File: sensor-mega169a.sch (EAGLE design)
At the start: 55 parts, among them IC3 ATmega169PA, K1 SP6029TOP, M1 NRF24L01P-M, M2 DHT22, Q1 IRLML2502, Q2 IRLML2502, Q3 IRLML6402, U1 MCP1640C, U2 MCP604-I/ST

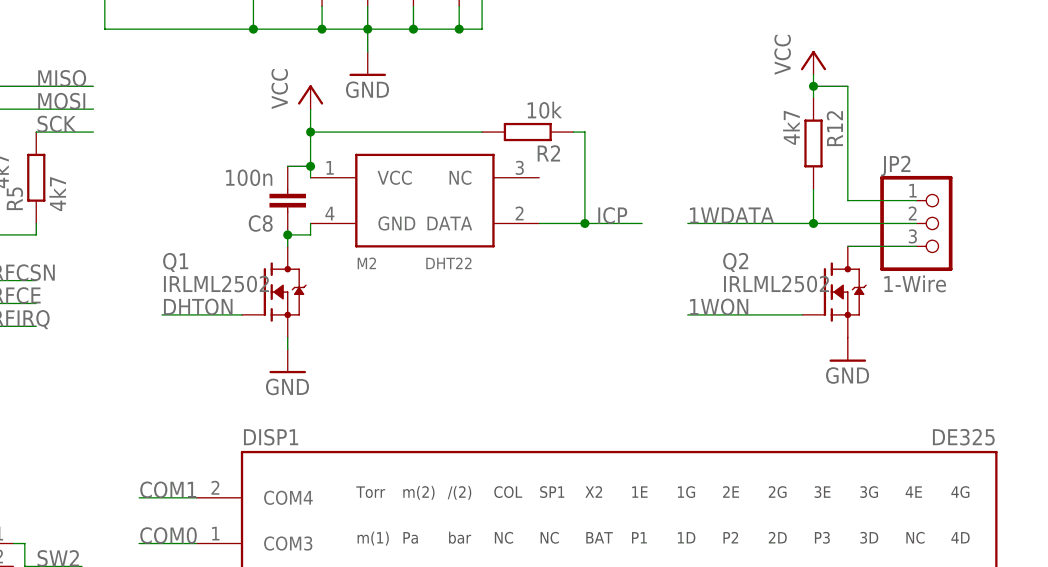
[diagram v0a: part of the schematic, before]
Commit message: changed irlml* parts to own library with better footprint
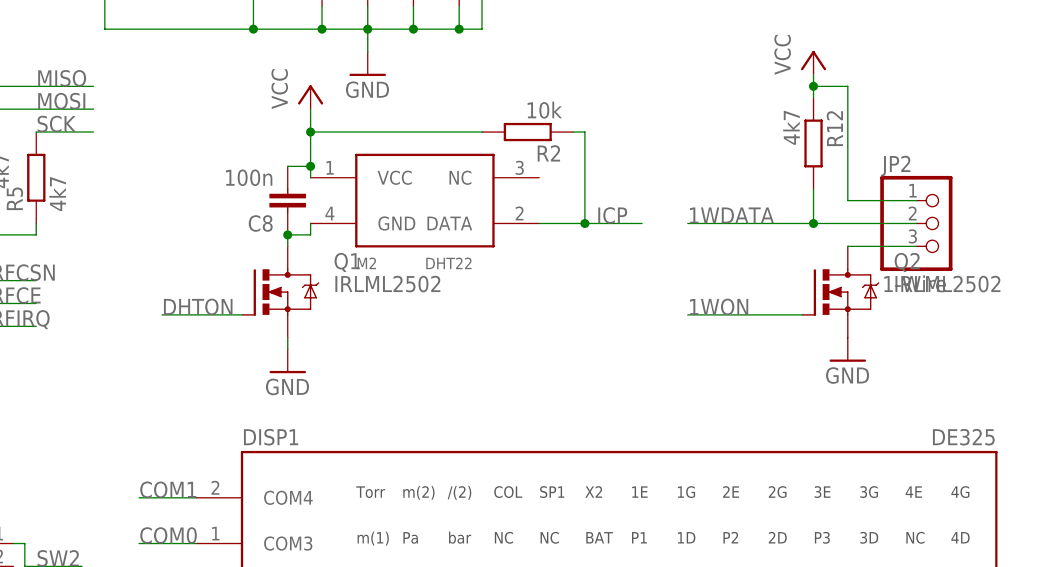
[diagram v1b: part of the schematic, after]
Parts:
- Q1, Q2: device xmaker:IRLML2502 -> mosfet:IRLML2502
- Q3: device transistor-power:IRLML5203 -> mosfet:IRLML6402
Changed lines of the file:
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@@
 <setting verticaltext="up"/>
 </settings>
-<grid distance="1.27" unitdist="mm" unit="mm" style="lines" multiple="1" display="yes" altdistance="635" altunitdist="mic" altunit="mic"/>
+<grid distance="0.1" unitdist="inch" unit="mm" style="lines" multiple="1" display="yes" altdistance="0.01" altunitdist="inch" altunit="mm"/>
 <layers>
-<layer number="1" name="Top" color="4" fill="1" visible="yes" active="no"/>
-<layer number="2" name="Route2" color="1" fill="3" visible="yes" active="no"/>
-<layer number="3" name="Route3" color="4" fill="3" visible="yes" active="no"/>
-<layer number="4" name="Route4" color="1" fill="4" visible="yes" active="no"/>
-<layer number="5" name="Route5" color="4" fill="4" visible="yes" active="no"/>
-<layer number="6" name="Route6" color="1" fill="8" visible="yes" active="no"/>
-<layer number="7" name="Route7" color="4" fill="8" visible="yes" active="no"/>
-<layer number="8" name="Route8" color="1" fill="2" visible="yes" active="no"/>
-<layer number="9" name="Route9" color="4" fill="2" visible="yes" active="no"/>
-<layer number="10" name="Route10" color="1" fill="7" visible="yes" active="no"/>
-<layer number="11" name="Route11" color="4" fill="7" visible="yes" active="no"/>
-<layer number="12" name="Route12" color="1" fill="5" visible="yes" active="no"/>
-<layer number="13" name="Route13" color="4" fill="5" visible="yes" active="no"/>
-<layer number="14" name="Route14" color="1" fill="6" visible="yes" active="no"/>
-<layer number="15" name="Route15" color="4" fill="6" visible="yes" active="no"/>
-<layer number="16" name="Bottom" color="1" fill="1" visible="yes" active="no"/>
-<layer number="17" name="Pads" color="2" fill="1" visible="yes" active="no"/>
-<layer number="18" name="Vias" color="2" fill="1" visible="yes" active="no"/>
-<layer number="19" name="Unrouted" color="6" fill="1" visible="yes" active="no"/>
-<layer number="20" name="Dimension" color="15" fill="1" visible="yes" active="no"/>
-<layer number="21" name="tPlace" color="7" fill="1" visible="yes" active="no"/>
-<layer number="22" name="bPlace" color="7" fill="1" visible="yes" active="no"/>
-<layer number="23" name="tOrigins" color="15" fill="1" visible="yes" active="no"/>
-<layer number="24" name="bOrigins" color="15" fill="1" visible="yes" active="no"/>
-<layer number="25" name="tNames" color="7" fill="1" visible="yes" active="no"/>
-<layer number="26" name="bNames" color="7" fill="1" visible="yes" active="no"/>
-<layer number="27" name="tValues" color="7" fill="1" visible="yes" active="no"/>
-<layer number="28" name="bValues" color="7" fill="1" visible="yes" active="no"/>
+<layer number="1" name="Top" color="4" fill="1" visible="no" active="no"/>
+<layer number="2" name="Route2" color="1" fill="3" visible="no" active="no"/>
+<layer number="3" name="Route3" color="4" fill="3" visible="no" active="no"/>
+<layer number="4" name="Route4" color="1" fill="4" visible="no" active="no"/>
+<layer number="5" name="Route5" color="4" fill="4" visible="no" active="no"/>
+<layer number="6" name="Route6" color="1" fill="8" visible="no" active="no"/>
+<layer number="7" name="Route7" color="4" fill="8" visible="no" active="no"/>
+<layer number="8" name="Route8" color="1" fill="2" visible="no" active="no"/>
+<layer number="9" name="Route9" color="4" fill="2" visible="no" active="no"/>
+<layer number="10" name="Route10" color="1" fill="7" visible="no" active="no"/>
+<layer number="11" name="Route11" color="4" fill="7" visible="no" active="no"/>
+<layer number="12" name="Route12" color="1" fill="5" visible="no" active="no"/>
+<layer number="13" name="Route13" color="4" fill="5" visible="no" active="no"/>
+<layer number="14" name="Route14" color="1" fill="6" visible="no" active="no"/>
+<layer number="15" name="Route15" color="4" fill="6" visible="no" active="no"/>
+<layer number="16" name="Bottom" color="1" fill="1" visible="no" active="no"/>
+<layer number="17" name="Pads" color="2" fill="1" visible="no" active="no"/>
+<layer number="18" name="Vias" color="2" fill="1" visible="no" active="no"/>
+<layer number="19" name="Unrouted" color="6" fill="1" visible="no" active="no"/>
+<layer number="20" name="Dimension" color="15" fill="1" visible="no" active="no"/>
+<layer number="21" name="tPlace" color="7" fill="1" visible="no" active="no"/>
+<layer number="22" name="bPlace" color="7" fill="1" visible="no" active="no"/>
+<layer number="23" name="tOrigins" color="15" fill="1" visible="no" active="no"/>
+<layer number="24" name="bOrigins" color="15" fill="1" visible="no" active="no"/>
+<layer number="25" name="tNames" color="7" fill="1" visible="no" active="no"/>
+<layer number="26" name="bNames" color="7" fill="1" visible="no" active="no"/>
+<layer number="27" name="tValues" color="7" fill="1" visible="no" active="no"/>
+<layer number="28" name="bValues" color="7" fill="1" visible="no" active="no"/>
 <layer number="29" name="tStop" color="7" fill="3" visible="no" active="no"/>
 <layer number="30" name="bStop" color="7" fill="6" visible="no" active="no"/>
@@
 <layer number="35" name="tGlue" color="7" fill="4" visible="no" active="no"/>
 <layer number="36" name="bGlue" color="7" fill="5" visible="no" active="no"/>
-<layer number="37" name="tTest" color="7" fill="1" visible="yes" active="no"/>
-<layer number="38" name="bTest" color="7" fill="1" visible="yes" active="no"/>
+<layer number="37" name="tTest" color="7" fill="1" visible="no" active="no"/>
+<layer number="38" name="bTest" color="7" fill="1" visible="no" active="no"/>
 <layer number="39" name="tKeepout" color="4" fill="11" visible="no" active="no"/>
 <layer number="40" name="bKeepout" color="1" fill="11" visible="no" active="no"/>
@@
 <layer number="44" name="Drills" color="7" fill="1" visible="no" active="no"/>
 <layer number="45" name="Holes" color="7" fill="1" visible="no" active="no"/>
-<layer number="46" name="Milling" color="3" fill="1" visible="yes" active="no"/>
-<layer number="47" name="Measures" color="7" fill="1" visible="yes" active="no"/>
-<layer number="48" name="Document" color="7" fill="1" visible="yes" active="no"/>
-<layer number="49" name="Reference" color="7" fill="1" visible="yes" active="no"/>
-<layer number="50" name="dxf" color="7" fill="1" visible="yes" active="no"/>
-<layer number="51" name="tDocu" color="7" fill="1" visible="yes" active="no"/>
-<layer number="52" name="bDocu" color="7" fill="1" visible="yes" active="no"/>
-<layer number="53" name="tGND_GNDA" color="7" fill="9" visible="yes" active="no"/>
-<layer number="54" name="bGND_GNDA" color="1" fill="9" visible="yes" active="no"/>
-<layer number="56" name="wert" color="7" fill="1" visible="yes" active="no"/>
+<layer number="46" name="Milling" color="3" fill="1" visible="no" active="no"/>
+<layer number="47" name="Measures" color="7" fill="1" visible="no" active="no"/>
+<layer number="48" name="Document" color="7" fill="1" visible="no" active="no"/>
+<layer number="49" name="Reference" color="7" fill="1" visible="no" active="no"/>
+<layer number="50" name="dxf" color="7" fill="1" visible="no" active="no"/>
+<layer number="51" name="tDocu" color="7" fill="1" visible="no" active="no"/>
+<layer number="52" name="bDocu" color="7" fill="1" visible="no" active="no"/>
+<layer number="53" name="tGND_GNDA" color="7" fill="9" visible="no" active="no"/>
+<layer number="54" name="bGND_GNDA" color="1" fill="9" visible="no" active="no"/>
+<layer number="56" name="wert" color="7" fill="1" visible="no" active="no"/>
 <layer number="91" name="Nets" color="2" fill="1" visible="yes" active="yes"/>
 <layer number="92" name="Busses" color="1" fill="1" visible="yes" active="yes"/>
@@
 <part name="R10" library="rcl" deviceset="R-EU_" device="R0603" value="270k"/>
 <part name="P+2" library="supply1" deviceset="VCC" device=""/>
-<part name="Q1" library="xmaker" deviceset="IRLML2502" device=""/>
+<part name="Q1" library="mosfet" deviceset="IRLML2502" device=""/>
 <part name="JP1" library="pinhead-mod" deviceset="PINHD-1X2" device="_2.54" value="I2C"/>
 <part name="JP2" library="pinhead-mod" deviceset="PINHD-1X3" device="_2.54" value="1-Wire"/>
@@
 <part name="R11" library="rcl" deviceset="R-EU_" device="R0603" value="4k7"/>
 <part name="P+5" library="supply1" deviceset="VCC" device=""/>
-<part name="Q2" library="xmaker" deviceset="IRLML2502" device=""/>
+<part name="Q2" library="mosfet" deviceset="IRLML2502" device=""/>
 <part name="GND1" library="supply1" deviceset="GND" device=""/>
 <part name="P+7" library="supply1" deviceset="VCC" device=""/>
@@
 <part name="R23" library="rcl" deviceset="R-EU_" device="R0201" value="0"/>
 <part name="R24" library="rcl" deviceset="R-EU_" device="R0201" value="0"/>
-<part name="Q3" library="transistor-power" deviceset="IRLML5203" device="" value="IRLML6402"/>
+<part name="Q3" library="mosfet" deviceset="IRLML6402" device="" value="IRLML6402"/>
 <part name="JP4" library="pinhead-mod" deviceset="PINHD-1X6" device="_2.54" value="ADC1"/>
 <part name="JP5" library="pinhead-mod" deviceset="PINHD-1X6" device="_2.54" value="ADC2"/>

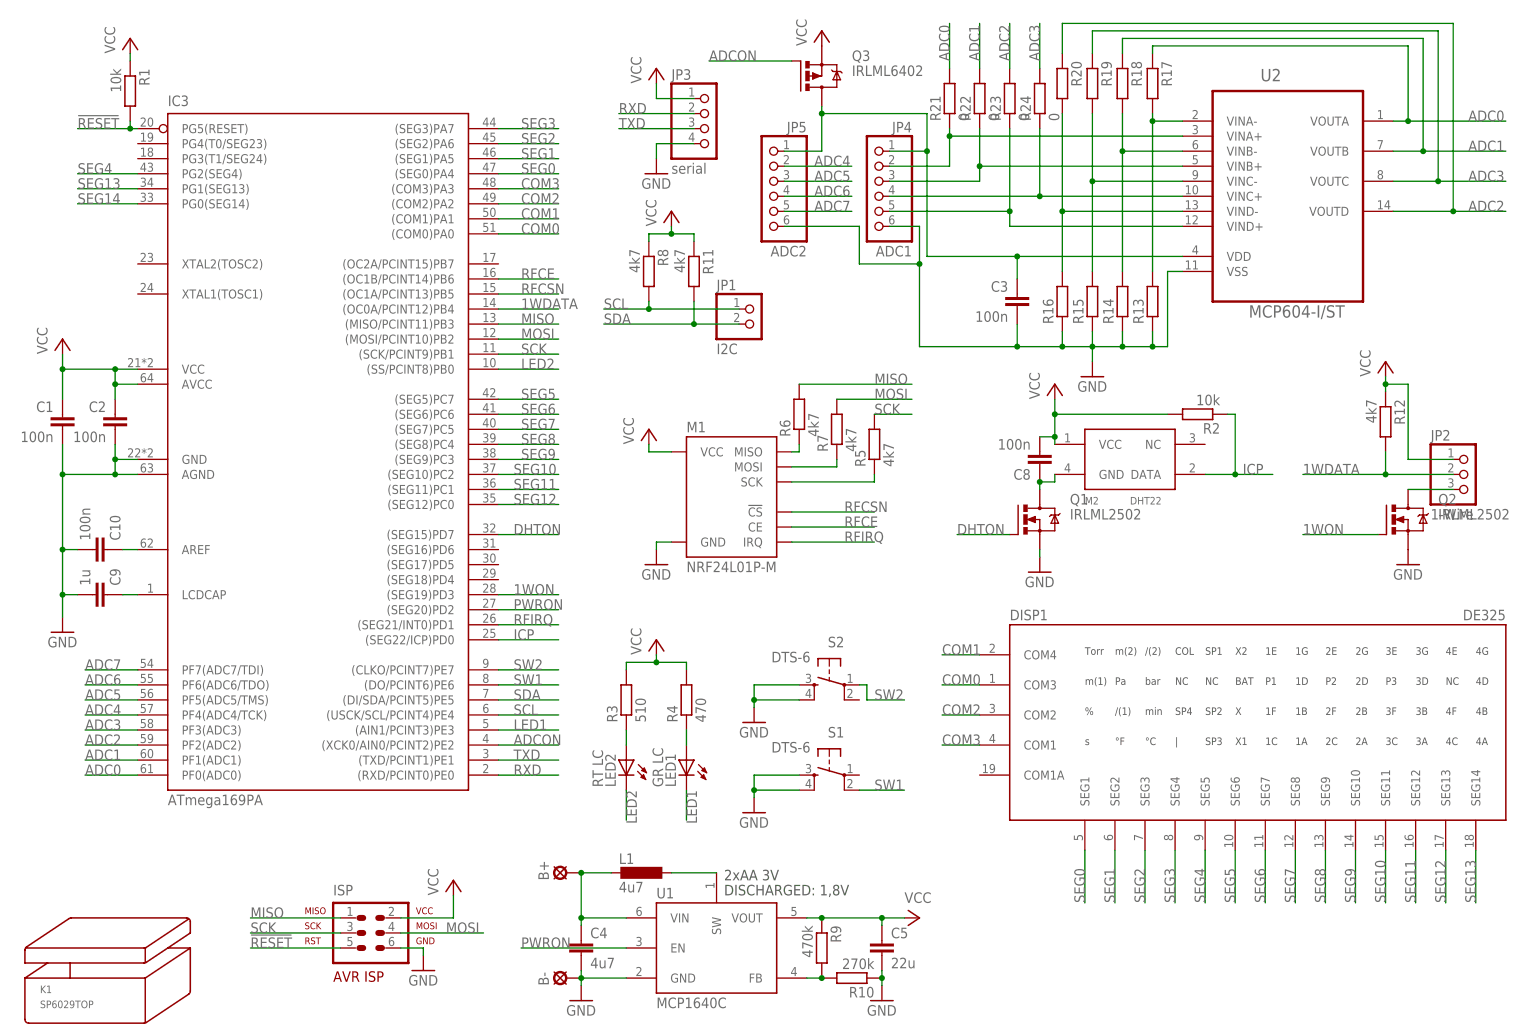
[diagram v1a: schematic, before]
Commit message: removed useless layers
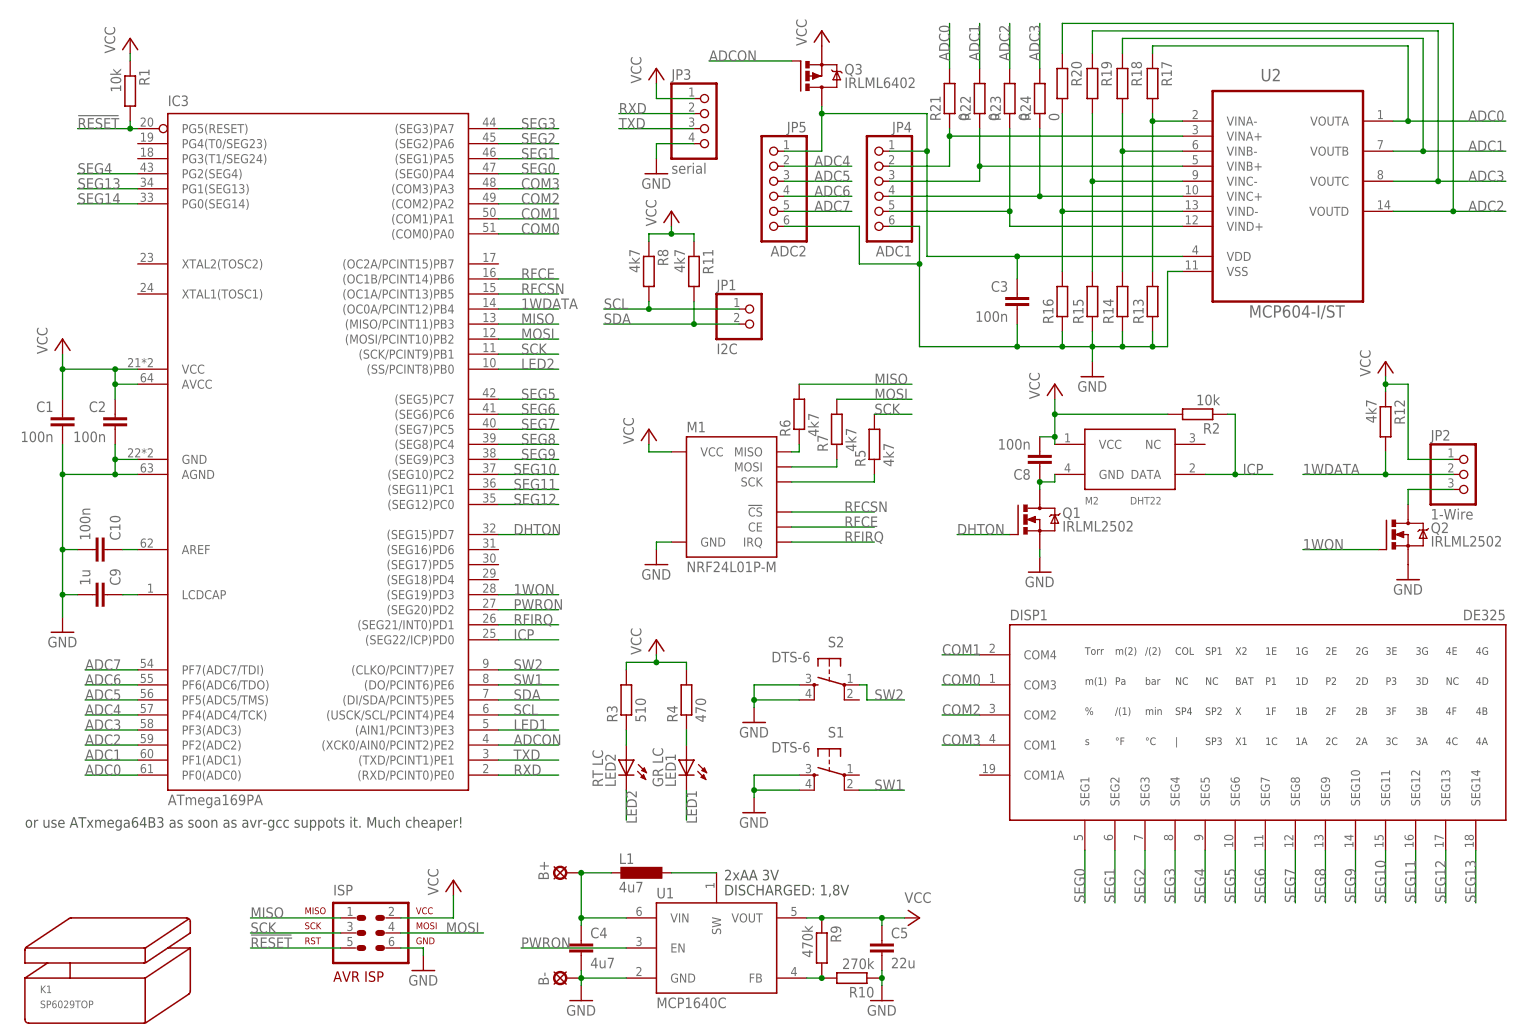
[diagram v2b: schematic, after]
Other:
- note added: "or use ATxmega64B3 as soon as avr-gcc suppots it. Much cheaper!"
- moved on the sheet: Q2
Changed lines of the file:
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@@
 <layer number="98" name="Guide" color="6" fill="1" visible="yes" active="yes"/>
 <layer number="100" name="Muster" color="7" fill="1" visible="no" active="no"/>
-<layer number="101" name="Patch_Top" color="12" fill="4" visible="no" active="yes"/>
-<layer number="102" name="Vscore" color="7" fill="1" visible="no" active="yes"/>
-<layer number="103" name="tMap" color="7" fill="1" visible="yes" active="yes"/>
-<layer number="104" name="Name" color="7" fill="1" visible="yes" active="yes"/>
-<layer number="105" name="tPlate" color="7" fill="1" visible="yes" active="yes"/>
-<layer number="106" name="bPlate" color="7" fill="1" visible="yes" active="yes"/>
-<layer number="107" name="Crop" color="7" fill="1" visible="yes" active="yes"/>
-<layer number="116" name="Patch_BOT" color="9" fill="4" visible="no" active="yes"/>
-<layer number="121" name="_tsilk" color="7" fill="1" visible="no" active="yes"/>
-<layer number="122" name="_bsilk" color="7" fill="1" visible="no" active="yes"/>
-<layer number="151" name="HeatSink" color="7" fill="1" visible="no" active="yes"/>
-<layer number="196" name="aValue" color="7" fill="1" visible="yes" active="yes"/>
 <layer number="200" name="200bmp" color="1" fill="10" visible="no" active="no"/>
-<layer number="201" name="201bmp" color="1" fill="10" visible="yes" active="yes"/>
-<layer number="202" name="202bmp" color="3" fill="10" visible="no" active="yes"/>
-<layer number="203" name="203bmp" color="4" fill="10" visible="no" active="yes"/>
-<layer number="204" name="204bmp" color="5" fill="10" visible="no" active="yes"/>
-<layer number="205" name="205bmp" color="6" fill="10" visible="no" active="yes"/>
-<layer number="206" name="206bmp" color="7" fill="10" visible="no" active="yes"/>
-<layer number="207" name="207bmp" color="8" fill="10" visible="no" active="yes"/>
-<layer number="208" name="208bmp" color="9" fill="10" visible="no" active="yes"/>
 <layer number="250" name="Descript" color="3" fill="1" visible="no" active="no"/>
 <layer number="251" name="SMDround" color="12" fill="11" visible="no" active="no"/>
-<layer number="254" name="cooling" color="7" fill="1" visible="no" active="yes"/>
 </layers>
 <schematic xreflabel="%F%N/%S.%C%R" xrefpart="/%S.%C%R">
@@
 <text x="123.19" y="29.21" size="1.778" layer="97">2xAA 3V</text>
 <text x="123.19" y="26.67" size="1.778" layer="97">DISCHARGED: 1,8V</text>
+<text x="5.08" y="38.1" size="1.778" layer="97">or use ATxmega64B3 as soon as avr-gcc suppots it. Much cheaper!</text>
 </plain>
 <instances>
@@
 <instance part="R11" gate="G$1" x="118.11" y="132.08" rot="R270"/>
 <instance part="P+5" gate="VCC" x="179.07" y="113.03"/>
-<instance part="Q2" gate="G$1" x="236.22" y="90.17"/>
-<instance part="GND1" gate="1" x="238.76" y="82.55"/>
+<instance part="Q2" gate="G$1" x="236.22" y="87.63"/>
+<instance part="GND1" gate="1" x="238.76" y="80.01"/>
 <instance part="P+7" gate="VCC" x="234.95" y="116.84"/>
 <instance part="R12" gate="G$1" x="234.95" y="106.68" rot="R270"/>
@@
 <segment>
 <pinref part="Q2" gate="G$1" pin="G"/>
-<wire x1="233.68" y1="87.63" x2="220.98" y2="87.63" width="0.1524" layer="91"/>
-<label x="220.98" y="87.63" size="1.778" layer="95"/>
+<wire x1="233.68" y1="85.09" x2="220.98" y2="85.09" width="0.1524" layer="91"/>
+<label x="220.98" y="85.09" size="1.778" layer="95"/>
 </segment>
 <segment>
@@
 <pinref part="Q2" gate="G$1" pin="D"/>
 <pinref part="JP2" gate="A" pin="3"/>
+<wire x1="238.76" y1="92.71" x2="238.76" y2="95.25" width="0.1524" layer="91"/>
 <wire x1="238.76" y1="95.25" x2="246.38" y2="95.25" width="0.1524" layer="91"/>
 </segment>
